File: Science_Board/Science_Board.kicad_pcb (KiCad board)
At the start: 2 copper layers, 217 x 149.5 mm, 139 parts, among them IC1 TCKE603RA, IC2 TCKE603RA, IC3 TCKE603RM, J1 Conn_01x02, J10 Conn_01x02, J11 Conn_01x03, J12 Conn_01x03, J13 Conn_01x03, J14 Conn_01x03, J15 Conn_01x03, J16 Conn_01x03, J17 Conn_01x03, J18 Conn_01x03, J19 Conn_01x02, J2 RJ45_LED_Shielded, J20 Molex_Megafit_02, J21 Molex_Megafit_02, J22 Molex_Megafit_02, J23 Conn_01x02, J3 Molex_Megafit_02, J4 Molex_Megafit_02, J5 Conn_01x05, J6 Conn_01x04, J7 Conn_01x03, J8 Conn_01x03, J9 Conn_01x02, Q1 BS250, Q2 NMOS, Q3 NMOS, Q4 NMOS, Q5 NMOS, SW1 SW_Push, SW10 SW_Push, SW11 SW_Push, SW12 SW_SPDT, SW2 SW_Push, SW3 SW_Push, SW4 SW_Push, SW5 SW_Push, SW6 SW_Push, SW7 SW_Push, SW8 SW_Push, SW9 SW_Push, U1 AP63205WU, U5 PCA9685PW

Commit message: Organizing layout
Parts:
- moved J15 223.9 mm to (49.5, 151.2), turned to -90 degrees
- moved Q1 213.7 mm to (66.0, 33.0)
- moved J16 209.3 mm to (64.8, 151.0), turned to -90 degrees
- moved J7 203.9 mm to (140.9, 147.3)
- moved D1 203.5 mm to (67.9, 42.5), turned to 180 degrees
- moved R1 202.2 mm to (67.6, 50.2), turned to 180 degrees
- moved J12 197.4 mm to (57.1, 151.0), turned to -90 degrees
- moved J9 196.3 mm to (116.1, 147.3)
- moved J17 194.5 mm to (81.3, 151.0), turned to -90 degrees
- moved C12 194.1 mm to (67.5, 55.9), turned to 180 degrees
- moved C13 192.6 mm to (67.5, 62.9)
- moved U1 191.6 mm to (82.5, 33.0)
- moved C1 189.7 mm to (76.6, 39.4)
- moved L1 185.2 mm to (88.0, 33.0)
- moved R28 183.6 mm to (216.2, 87.5)
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
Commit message: Finish Very Rough Layout
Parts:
- moved J20 130.7 mm to (51.0, 92.0), turned to -90 degrees
- moved IC3 128.1 mm to (77.5, 116.5), turned to -90 degrees
- moved D11 110.1 mm to (92.7, 115.6), turned to 180 degrees
- moved R10 109.0 mm to (90.2, 118.7), turned to -90 degrees
- moved C9 108.2 mm to (82.5, 116.6), turned to -90 degrees
- moved D13 106.1 mm to (93.0, 102.9), turned to 180 degrees
- moved IC1 105.5 mm to (77.5, 103.8), turned to -90 degrees
- moved R24 105.3 mm to (94.0, 119.7), turned to -90 degrees
- moved R9 104.6 mm to (85.7, 118.4), turned to 90 degrees
- moved R5 103.0 mm to (85.7, 105.7), turned to 90 degrees
- moved C5 102.5 mm to (82.5, 103.9), turned to -90 degrees
- moved R47 101.4 mm to (94.0, 107.0), turned to -90 degrees
- moved C8 100.9 mm to (73.0, 116.6), turned to -90 degrees
- moved Q2 99.8 mm to (103.0, 106.0)
- moved R6 99.1 mm to (90.2, 105.8), turned to -90 degrees
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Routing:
- net GND: vias 1 -> 0

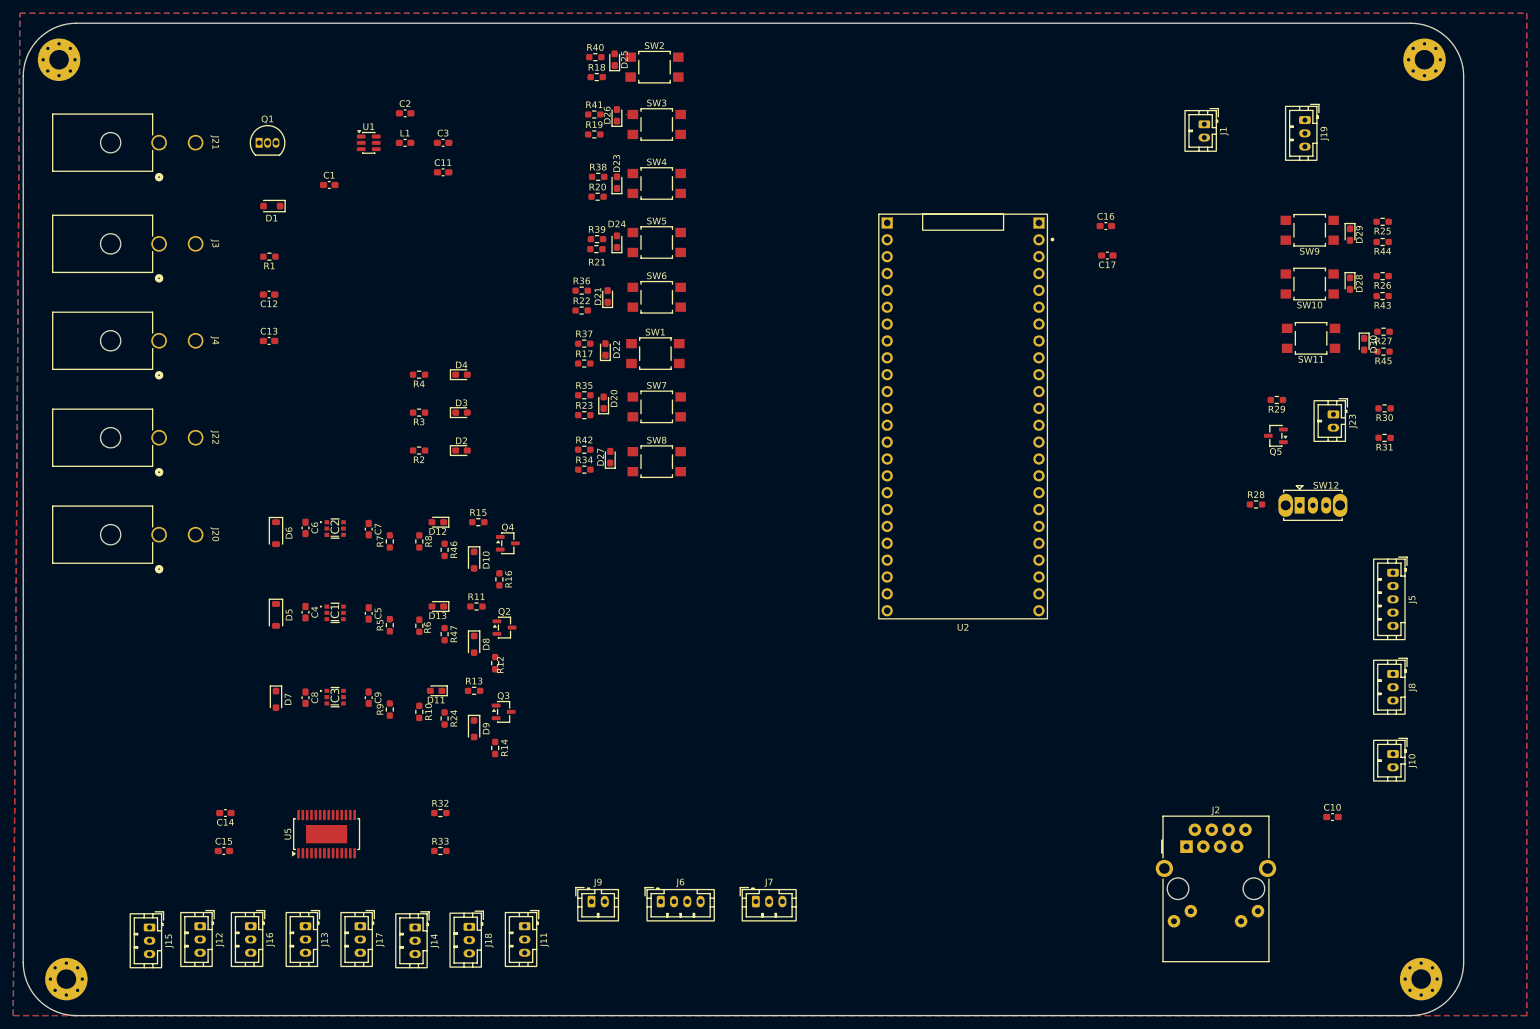
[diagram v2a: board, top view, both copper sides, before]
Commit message: Working on compacting layout
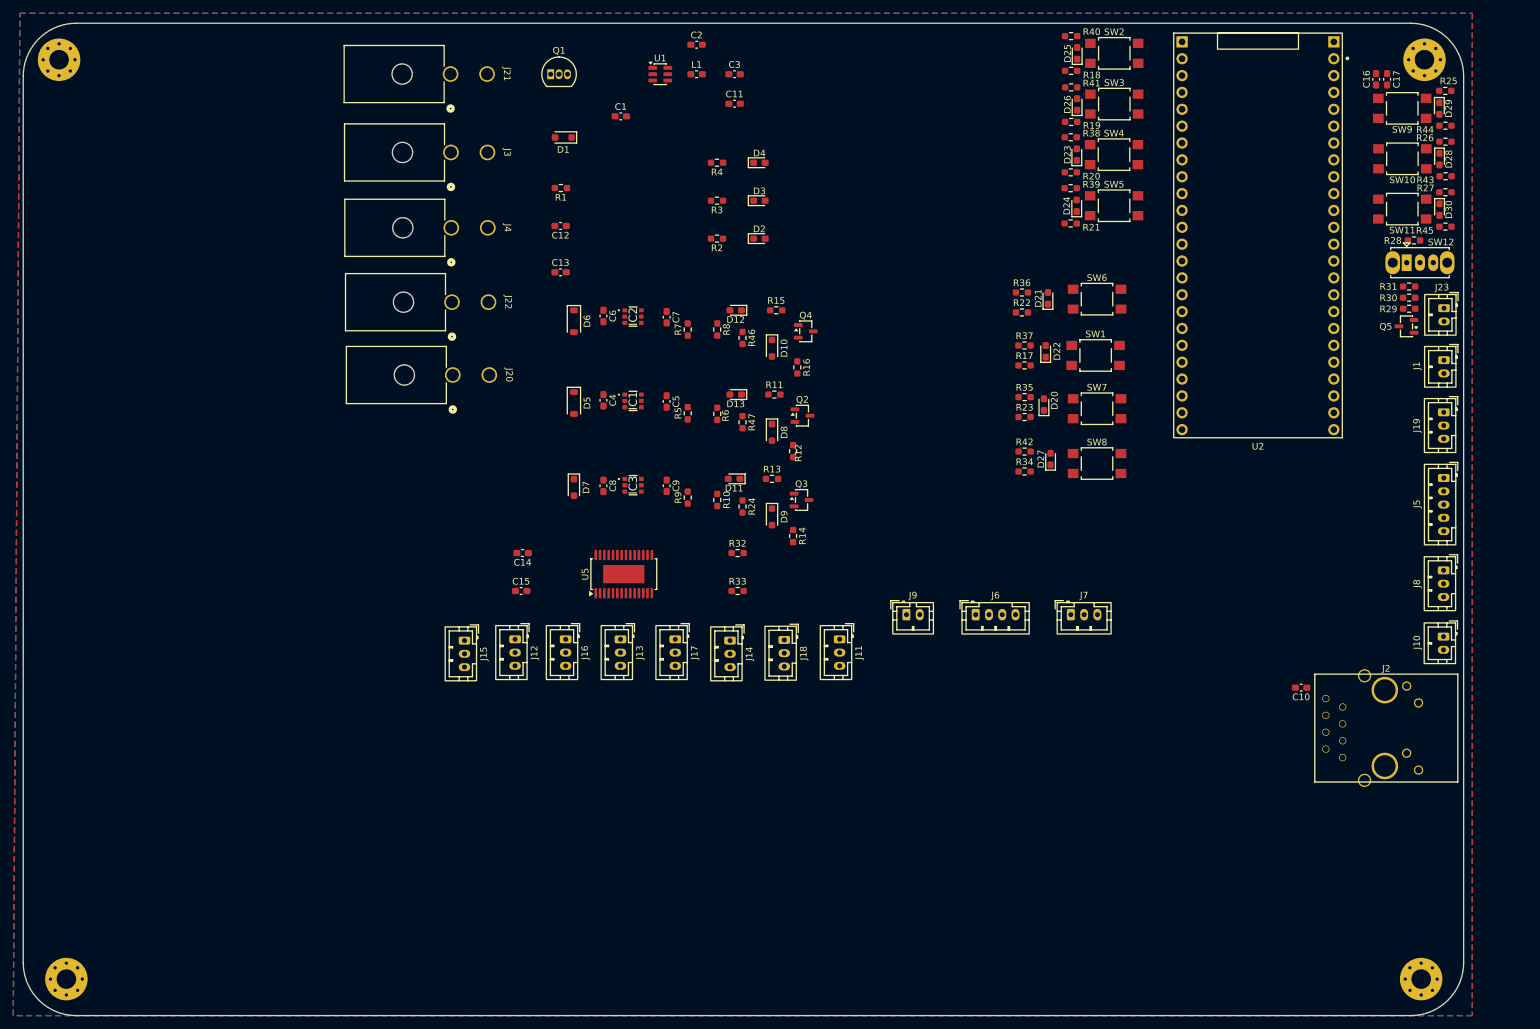
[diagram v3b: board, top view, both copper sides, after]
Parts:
- J2: footprint Connector_RJ:RJ45_Amphenol_RJMG1BD3B8K1ANR -> MRDT_Connectors:RJ45_Teensy
- moved R41 72.0 mm to (188.4, 24.7)
- moved R19 71.9 mm to (188.4, 29.9)
- moved R39 71.8 mm to (188.3, 39.9)
- moved R40 71.7 mm to (188.4, 16.9)
- moved R21 71.5 mm to (188.3, 45.2)
- moved R18 71.5 mm to (188.4, 22.2)
- moved R38 71.4 mm to (188.3, 32.2)
- moved R20 71.4 mm to (188.3, 37.5)
- moved D25 69.7 mm to (189.3, 19.5)
- moved D24 69.5 mm to (189.2, 42.5)
- moved D23 69.4 mm to (189.2, 34.8)
- moved D26 69.3 mm to (189.3, 27.2)
- moved SW2 69.3 mm to (194.9, 19.5)
- moved SW5 69.1 mm to (194.8, 42.5)
- moved SW4 69.0 mm to (194.8, 34.8)
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
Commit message: more layout condensing
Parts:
- removed C1: 10uF, Capacitor_SMD:C_0603_1608Metric_Pad1.08x0.95mm_HandSolder
- removed C11: 22uF, Capacitor_SMD:C_0603_1608Metric_Pad1.08x0.95mm_HandSolder
- removed U1: AP63205WU, Package_TO_SOT_SMD:TSOT-23-6
- added C19: 22uF, Capacitor_SMD:C_0603_1608Metric_Pad1.08x0.95mm_HandSolder, F.Cu at (185.1, 34.8)
- added C20: 6.8uF, Capacitor_SMD:C_0603_1608Metric_Pad1.08x0.95mm_HandSolder, F.Cu at (183.5, 34.8)
- added C21: 6.8uF, Capacitor_SMD:C_0603_1608Metric_Pad1.08x0.95mm_HandSolder, F.Cu at (181.8, 34.8)
- added D14: 28V, Diode_SMD:D_SOD-123, F.Cu at (176.4, 36.0)
- added U3: LM22678TJ-5, Package_TO_SOT_SMD:TO-263-7_TabPin8, F.Cu at (180.2, 22.7)
- C2: value 100nF -> 10nF
- C3: value 22uF -> 180uF
- L1: value 4.7uH -> 6.8uH; footprint Inductor_SMD:L_0603_1608Metric_Pad1.05x0.95mm_HandSolder -> Inductor_SMD:L_Bourns_SRN8040TA
- Q1: footprint Package_TO_SOT_THT:TO-92_Inline -> Package_TO_SOT_SMD:SOT-223
- moved L1 50.3 mm to (178.5, 41.7)
- moved C2 46.4 mm to (175.7, 33.9)
- moved C3 43.0 mm to (179.2, 33.9), turned to 180 degrees
- moved R4 36.4 mm to (165.7, 55.5), turned to 0 degrees
- moved R3 32.4 mm to (165.7, 52.0), turned to 0 degrees
- moved C13 32.0 mm to (112.0, 20.6), turned to -90 degrees
- moved R2 30.7 mm to (165.7, 48.5), turned to 0 degrees
- moved D4 30.1 mm to (165.7, 53.8)
- moved D3 25.8 mm to (165.7, 50.3)
- moved C12 25.1 mm to (113.7, 20.6), turned to 90 degrees
- moved D2 24.3 mm to (165.7, 46.8)
- moved R33 21.0 mm to (118.8, 92.2), turned to 90 degrees
- moved R16 18.9 mm to (136.8, 51.1), turned to 180 degrees
- moved R12 18.4 mm to (136.9, 63.8), turned to 180 degrees
- moved R14 18.4 mm to (136.6, 76.7), turned to 180 degrees
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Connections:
- J21 pad 1: Net-(Q1-D) -> Net-(J21-Pad1)
- Q1 pad 1: Net-(Q1-D) -> Net-(D1-A)
- Q1 pad 2: Net-(D1-A) -> Net-(J21-Pad1)

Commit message: mor layot
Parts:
- moved H3 131.6 mm to (164.5, 126.3)
- moved J20 128.1 mm to (214.5, 114.8), turned to 0 degrees
- moved J22 123.3 mm to (204.0, 114.8), turned to 0 degrees
- moved J21 120.7 mm to (172.9, 114.8), turned to 0 degrees
- moved J4 120.4 mm to (193.6, 114.7), turned to 0 degrees
- moved J3 119.3 mm to (183.2, 114.7), turned to 0 degrees
- moved Q1 104.1 mm to (173.1, 103.0), turned to -90 degrees
- moved C13 97.0 mm to (170.8, 97.7), turned to 0 degrees
- moved D1 96.1 mm to (174.7, 97.5), turned to 0 degrees
- moved C12 94.6 mm to (170.8, 96.0), turned to 180 degrees
- moved R1 93.4 mm to (175.0, 95.6), turned to 0 degrees
- moved J9 81.3 mm to (244.4, 95.9), turned to -90 degrees
- moved C5 81.1 mm to (123.8, 143.2)
- moved D10 81.1 mm to (127.4, 134.2)
- moved D13 81.1 mm to (126.5, 144.0)
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
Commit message: More layout
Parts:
- moved J15 145.7 mm to (160.5, 49.2), turned to 90 degrees
- moved J12 133.3 mm to (160.4, 59.3), turned to 90 degrees
- moved C15 127.4 mm to (184.7, 76.3)
- moved C14 127.4 mm to (186.4, 76.3)
- moved R32 127.4 mm to (189.8, 76.3)
- moved R33 127.4 mm to (188.1, 76.3)
- moved U5 124.2 mm to (187.3, 83.3), turned to 0 degrees
- moved J16 120.9 mm to (160.4, 69.5), turned to 90 degrees
- moved J13 108.2 mm to (160.4, 79.5), turned to 90 degrees
- moved Q4 62.4 mm to (133.2, 72.1), turned to 90 degrees
- moved R16 59.4 mm to (130.6, 72.5), turned to -90 degrees
- moved D10 59.1 mm to (132.9, 75.3), turned to 180 degrees
- moved R15 57.1 mm to (132.5, 77.2), turned to 0 degrees
- moved R8 55.8 mm to (132.7, 78.9), turned to 180 degrees
- moved D12 55.1 mm to (130.0, 76.3), turned to -90 degrees
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
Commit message: Layout changes
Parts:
- moved H2 160.6 mm to (87.8, 66.9), turned to 90 degrees
- moved C17 153.0 mm to (94.1, 68.9), turned to 0 degrees
- moved C16 151.9 mm to (94.1, 70.6), turned to 180 degrees
- moved U2 150.9 mm to (84.1, 101.7), turned to 90 degrees
- moved R28 148.6 mm to (97.6, 68.9), turned to 180 degrees
- moved SW12 148.4 mm to (99.9, 65.5), turned to 180 degrees
- moved R44 147.0 mm to (85.2, 116.5), turned to 90 degrees
- moved SW9 144.0 mm to (87.8, 110.0), turned to 90 degrees
- moved D29 143.4 mm to (87.8, 115.6), turned to 180 degrees
- moved R31 143.4 mm to (101.4, 69.8), turned to 90 degrees
- moved R30 141.4 mm to (103.0, 69.8), turned to 90 degrees
- moved J23 140.5 mm to (106.6, 65.3), turned to 0 degrees
- moved R25 139.6 mm to (90.4, 116.5), turned to 90 degrees
- moved R29 137.3 mm to (106.0, 70.5), turned to 90 degrees
- moved R43 136.3 mm to (92.8, 116.5), turned to 90 degrees
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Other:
- board size 217 x 149.5 mm -> 117.1 x 84.4 mm

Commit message: layout look better
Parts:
- added J24: Conn_01x02, Connector_JST:JST_PH_B2B-PH-K_1x02_P2.00mm_Vertical, F.Cu at (163.4, 65.4)
- added Q6: NMOS, Package_TO_SOT_SMD:SOT-23-3, F.Cu at (169.9, 65.2)
- added R48: 100, Resistor_THT:R_Array_SIP4, F.Cu at (173.5, 68.1)
- added R49: 10k, Resistor_THT:R_Array_SIP4, F.Cu at (173.5, 64.6)
- moved J7 108.0 mm to (86.5, 111.8), turned to 90 degrees
- moved J6 103.6 mm to (86.5, 123.8), turned to 90 degrees
- moved J9 102.1 mm to (86.5, 131.8), turned to 90 degrees
- moved R44 76.1 mm to (160.1, 102.9), turned to 180 degrees
- moved D29 73.0 mm to (159.2, 100.3), turned to -90 degrees
- moved R25 72.1 mm to (160.1, 97.7), turned to 180 degrees
- moved R43 70.6 mm to (160.1, 95.3), turned to 180 degrees
- moved D28 67.8 mm to (159.2, 92.8), turned to -90 degrees
- moved R26 67.4 mm to (160.1, 90.1), turned to 180 degrees
- moved SW9 66.5 mm to (153.6, 100.3), turned to 180 degrees
- moved R45 66.3 mm to (160.1, 87.8), turned to 180 degrees
- moved R27 64.2 mm to (160.1, 82.6), turned to 180 degrees
- moved D30 64.0 mm to (159.2, 85.2), turned to -90 degrees
- moved SW10 60.7 mm to (153.6, 92.7), turned to 180 degrees
- moved SW11 56.4 mm to (153.6, 85.1), turned to 180 degrees
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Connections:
- J20 pad 1: +PV -> +Vpre
- J21 pad 1: Net-(J21-Pad1) -> +Vpre
- J3 pad 1: +PV -> +Vpre
- J4 pad 1: +PV -> +Vpre
- Q1 pad 2: Net-(J21-Pad1) -> +Vpre
- Q1 pad 4: Net-(J21-Pad1) -> +Vpre
- U2 pad 42: unconnected-(U2-PB0-Pad42) -> TEMP_CONTROL
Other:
- board size 117.1 x 84.4 mm -> 108.3 x 85.5 mm
